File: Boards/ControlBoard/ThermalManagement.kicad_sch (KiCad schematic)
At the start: 42 parts, among them J24 5442251, J5 5442251, J7 5442251, J8 5442251, J9 5442251, M1 Fan_4pin, M2 Fan_4pin, M3 Fan_4pin, M4 Fan_4pin, M5 Fan_4pin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

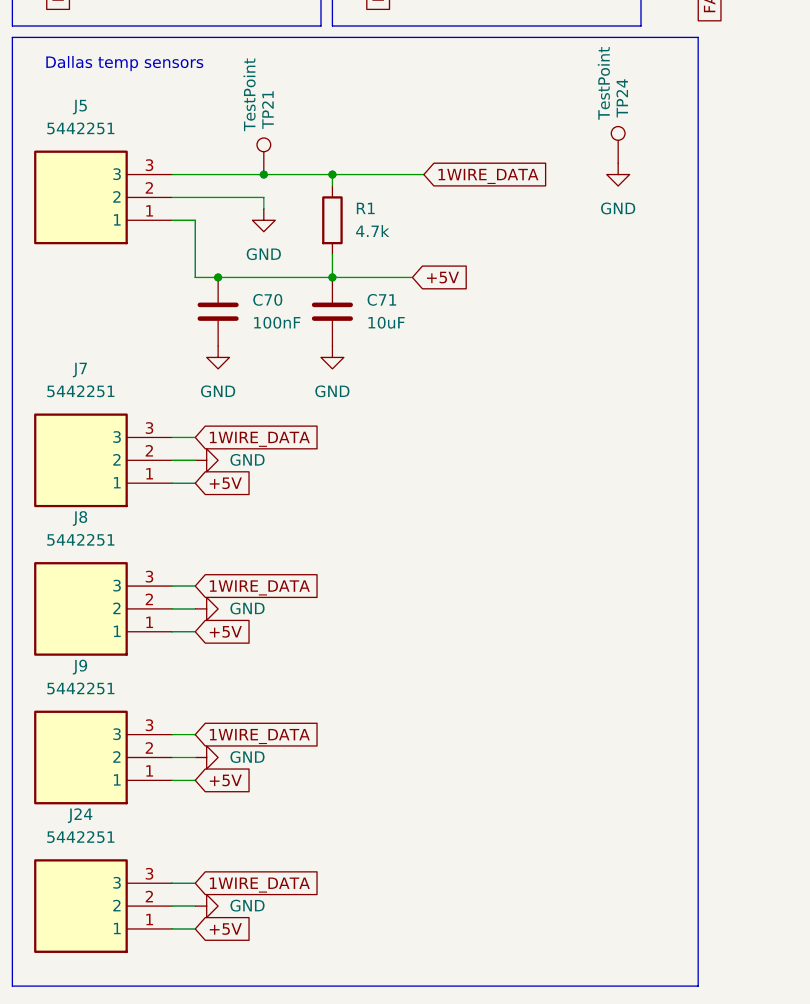
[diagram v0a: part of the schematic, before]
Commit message: Update control board
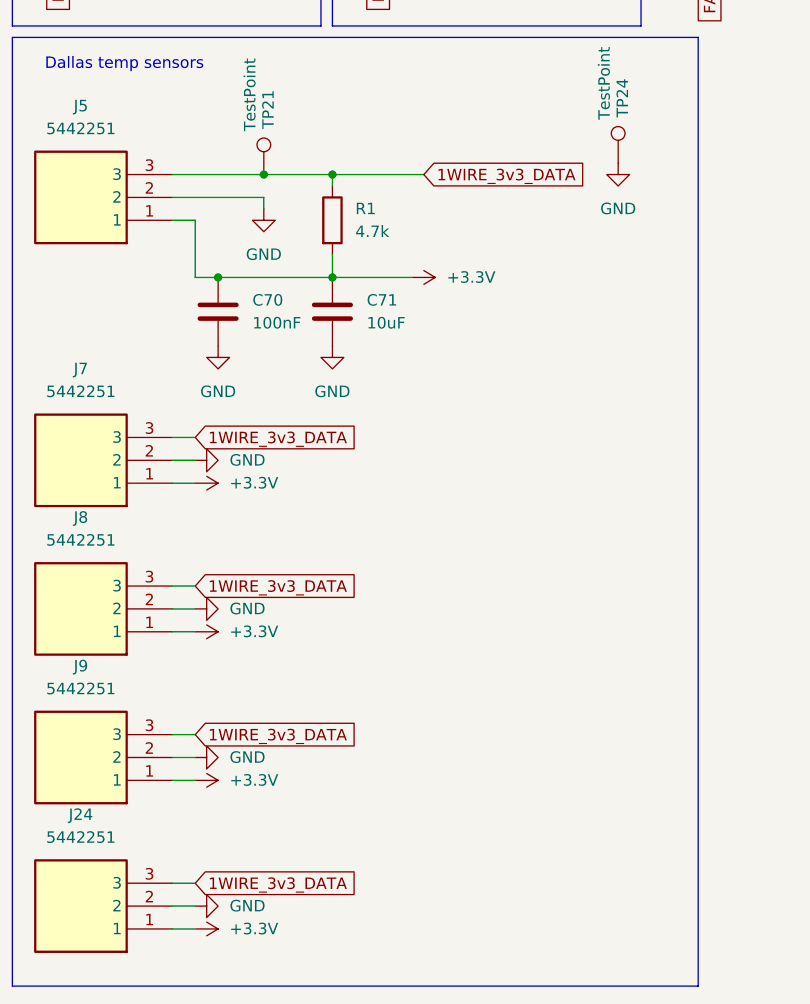
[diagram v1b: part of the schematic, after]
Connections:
- net +5V renamed +3.3V
- net 1WIRE_DATA renamed 1WIRE_3v3_DATA
